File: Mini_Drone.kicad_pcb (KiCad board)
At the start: 4 copper layers, 55 x 50.7 mm, 82 parts, among them J1 Conn_01x02, J3 Conn_01x02, J4 Conn_01x06, J7 Conn_01x11, J8 Conn_01x11, Q1 AO3400A, Q2 AO3400A, Q3 AO3400A, Q4 AO3400A, U1 ESP32-S3-WROOM-1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

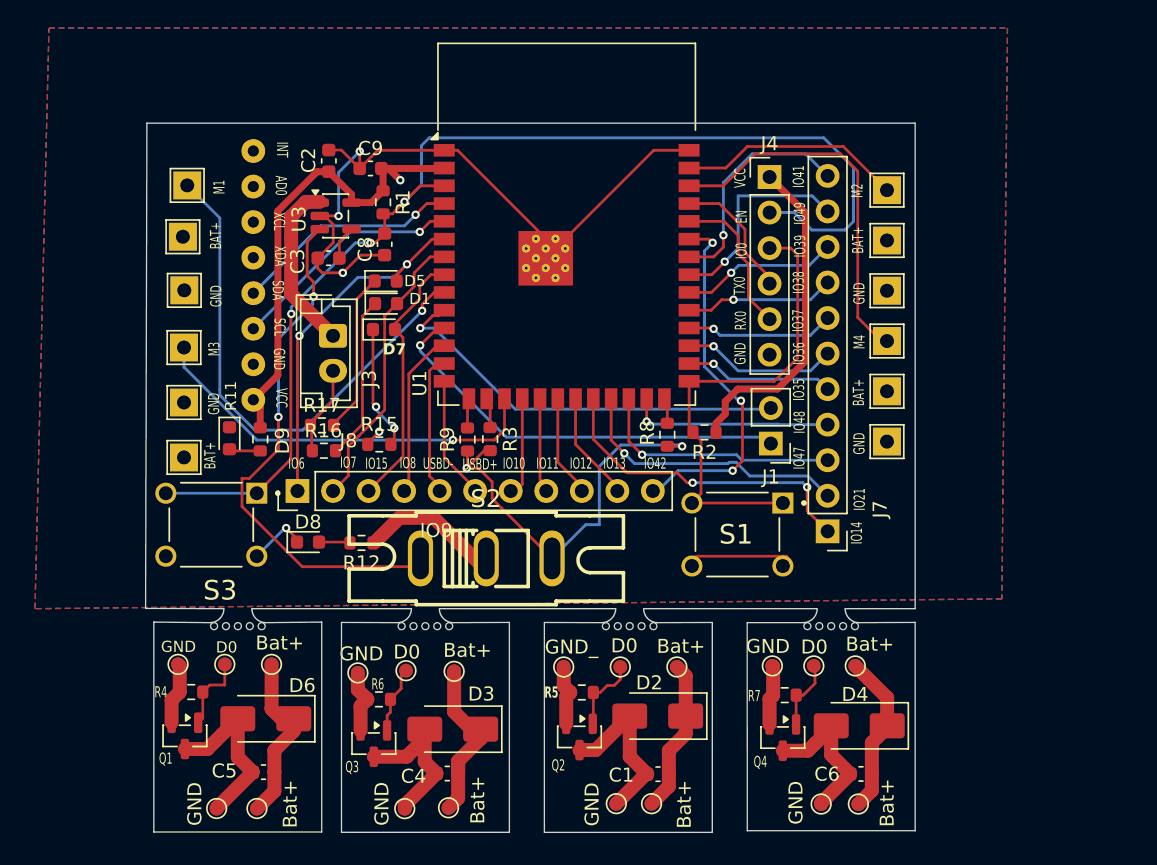
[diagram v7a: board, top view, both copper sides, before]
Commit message: switch connection has been corrected and the  polygon pour  has been reduced  to one layer for gnd and the connection is set to thermaal relief  for  easier soldering
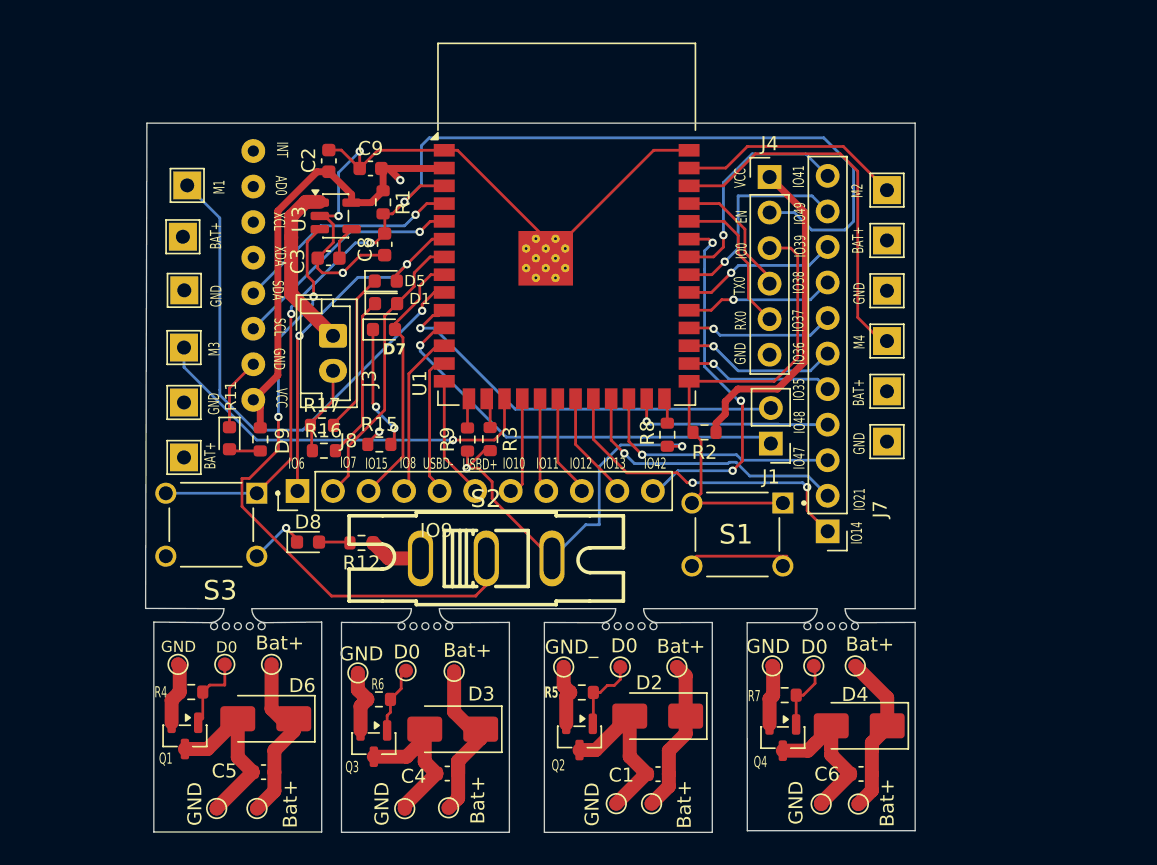
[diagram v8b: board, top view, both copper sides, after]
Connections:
- S2 pad 1: Net-(U3-EN) -> /BAT+
- S2 pad 2: /BAT+ -> Net-(U3-EN)
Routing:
- net Net-(U3-EN): track 38.3 -> 45.2 mm
- net GND: track 100.0 -> 105.2 mm
- net /BAT+: track 35.7 -> 30.9 mm
- removed copper zone on B.Cu, net GND
- removed copper zone on F.Cu, net GND
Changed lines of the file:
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@@
 			(layers "*.Cu" "*.Mask")
 			(remove_unused_layers no)
-			(net 64 "Net-(U3-EN)")
+			(net 5 "/BAT+")
 			(pintype "passive")
 			(solder_mask_margin 0.0508)
@@
 			(layers "*.Cu" "*.Mask")
 			(remove_unused_layers no)
-			(net 5 "/BAT+")
+			(net 64 "Net-(U3-EN)")
 			(pintype "passive")
 			(solder_mask_margin 0.0508)
@@
 	)
 	(segment
+		(start 196.9 90.235)
+		(end 198.6025 88.5325)
+		(width 0.2)
+		(layer "F.Cu")
+		(net 2)
+	)
+	(segment
 		(start 219.5 79.54)
 		(end 219.5 80.96)
@@
 	)
 	(segment
+		(start 196.9 93.0325)
+		(end 196.9 90.235)
+		(width 0.2)
+		(layer "F.Cu")
+		(net 2)
+	)
+	(segment
 		(start 215.67 98.13)
 		(end 219.95 102.41)
@@
 	)
 	(segment
-		(start 201.31 79.46)
-		(end 201.31 77.97)
-		(width 1)
+		(start 210.3 101.8)
+		(end 210.3 103)
+		(width 0.2)
 		(layer "F.Cu")
 		(net 5)
 	)
 	(segment
-		(start 207.35 101.2)
-		(end 209.04 99.51)
+		(start 208.27 102.41)
+		(end 207.16 101.3)
 		(width 1)
 		(layer "F.Cu")
@@
 	)
 	(segment
-		(start 211.51 99.51)
-		(end 215 103)
+		(start 201.31 79.46)
+		(end 201.31 77.97)
 		(width 1)
 		(layer "F.Cu")
@@
 	)
 	(segment
-		(start 209.04 99.51)
-		(end 211.51 99.51)
+		(start 210.552 102.41)
+		(end 208.27 102.41)
 		(width 1)
 		(layer "F.Cu")
@@
 	)
 	(segment
-		(start 202.1 103)
+		(start 214.51 105.1)
+		(end 214.51 105.06)
+		(width 0.2)
+		(layer "F.Cu")
+		(net 64)
+	)
+	(segment
+		(start 197.795 96.695)
 		(end 197.795 98.695)
 		(width 0.2)
@@
 	)
 	(segment
-		(start 210.3 101.8)
-		(end 210.3 103)
+		(start 204.2 105.1)
+		(end 214.51 105.1)
+		(width 0.2)
+		(layer "F.Cu")
+		(net 64)
+	)
+	(segment
+		(start 200.4 94.614064)
+		(end 198.319064 96.695)
 		(width 0.2)
 		(layer "F.Cu")
@@
 	)
 	(segment
-		(start 200.4 94.614064)
-		(end 200.4 92.3)
+		(start 215.251 104.319)
+		(end 215.251 102.41)
 		(width 0.2)
 		(layer "F.Cu")
@@
 	)
 	(segment
-		(start 210.3 103)
-		(end 202.1 103)
+		(start 200.4 92.3)
+		(end 200.4 94.614064)
 		(width 0.2)
 		(layer "F.Cu")
@@
 	)
 	(segment
-		(start 198.319064 96.695)
-		(end 200.4 94.614064)
+		(start 197.795 98.695)
+		(end 204.2 105.1)
 		(width 0.2)
 		(layer "F.Cu")
@@
 	)
 	(segment
-		(start 197.795 96.695)
-		(end 198.319064 96.695)
+		(start 214.51 105.06)
+		(end 215.251 104.319)
 		(width 0.2)
 		(layer "F.Cu")
@@
 	)
 	(segment
-		(start 197.795 98.695)
+		(start 198.319064 96.695)
 		(end 197.795 96.695)
 		(width 0.2)
@@
 		(net 2)
 		(net_name "GND")
-		(layers "F.Cu" "B.Cu")
-		(hatch edge 0.5)
-		(priority 2)
-		(connect_pads yes
-			(clearance 0.5)
-		)
-		(min_thickness 0.25)
-		(filled_areas_thickness no)
-		(fill yes
-			(thermal_gap 0.5)
-			(thermal_bridge_width 0.5)
-		)
-		(polygon
-			(pts
-				(xy 184 64.5) (xy 252.5 64.5) (xy 252.1 105.3) (xy 183 106)
-			)
-		)
-	)
-	(zone
-		(net 2)
-		(net_name "GND")
 		(layer "In1.Cu")
 		(hatch edge 0.5)
-		(connect_pads yes
+		(connect_pads
 			(clearance 0.5)
 		)
@@
 		(polygon
 			(pts
-				(xy 189.2 67.84) (xy 248 68) (xy 246.4 105.4) (xy 186.9 105.9) (xy 189.38 67.93) (xy 191.46 66.93)
+				(xy 189.18 67.83) (xy 248 68) (xy 246.4 105.4) (xy 186.9 105.9) (xy 189.16 68.02) (xy 189.17 67.92)
 			)
 		)
@@
 		(polygon
 			(pts
-				(xy 185.99 64.78) (xy 250 66) (xy 249.2 105.2) (xy 186.6 106) (xy 187.46 62.74)
+				(xy 185.99 64.78) (xy 250 66) (xy 249.23 105.36) (xy 186.6 106) (xy 186 65.12)
 			)
 		)
